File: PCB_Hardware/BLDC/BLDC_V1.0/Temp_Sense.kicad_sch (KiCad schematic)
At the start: 2 parts

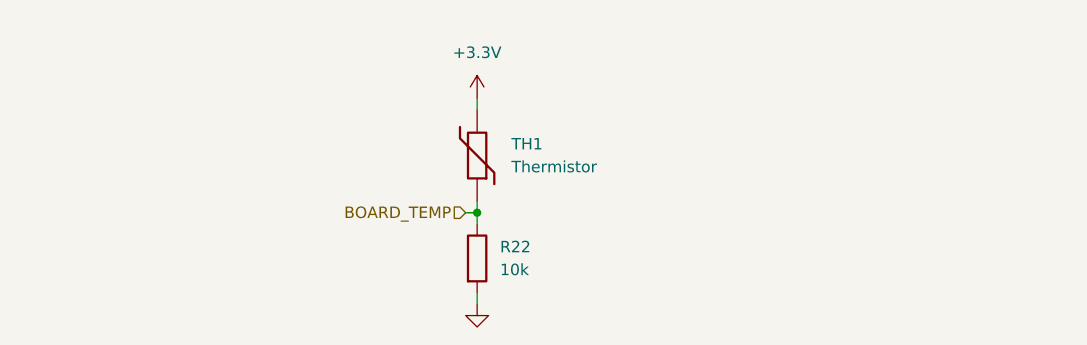
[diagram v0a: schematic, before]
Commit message: redid external temp sensing and instead removed V Bus sense from the USBC input
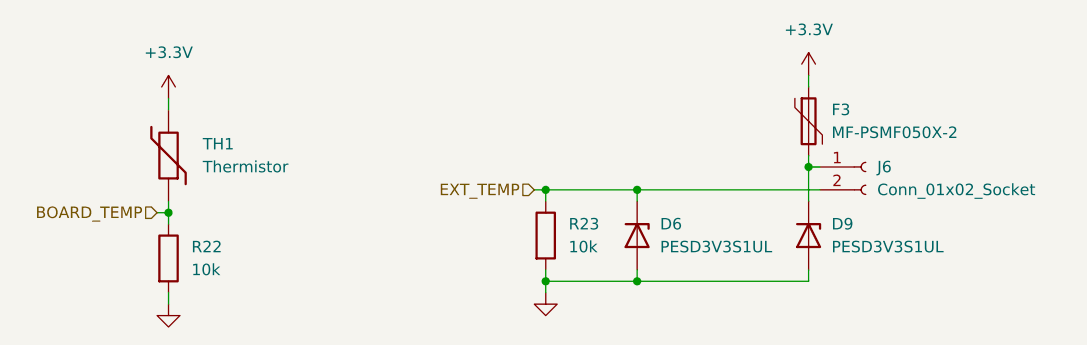
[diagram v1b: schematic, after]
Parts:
- added D6, D9: PESD3V3S1UL, Diode_SMD:D_SOD-882, symbol Diode:PESD3V3S1UL
- added F3: MF-PSMF050X-2, symbol Device:Polyfuse
- added J6: Conn_01x02_Socket, symbol Connector:Conn_01x02_Socket
- added R23: 10k, symbol Device:R
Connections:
- net +3.3V: now also F3.1
- net GND: now also D6.2 (A), D9.2 (A), R23.2
- new net: D9.1 (K), F3.2, J6.1 (Pin_1)
- new net EXT_TEMP: D6.1 (K), J6.2 (Pin_2), R23.1
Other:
- moved on the sheet: R22, TH1

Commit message: Removed external temp sensing bc I forgot the calibration enable pin for the encoder
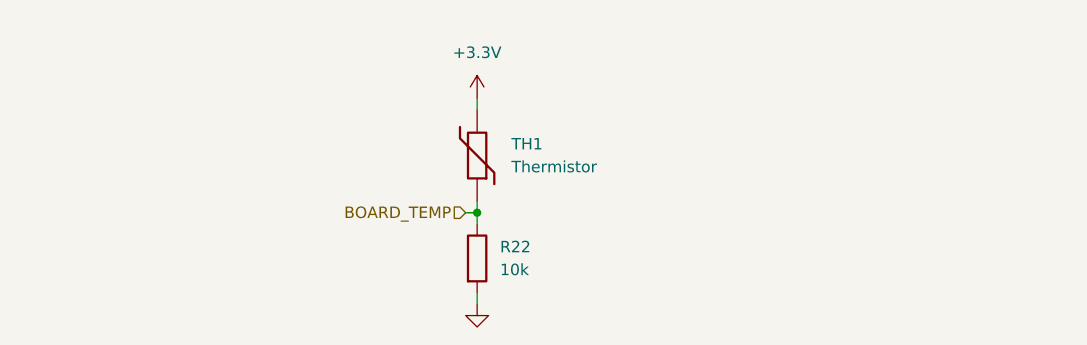
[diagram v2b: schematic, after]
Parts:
- removed D6, D9: PESD3V3S1UL, Diode_SMD:D_SOD-882, symbol Diode:PESD3V3S1UL
- removed F3: MF-PSMF050X-2, symbol Device:Polyfuse
- removed J6: Conn_01x02_Socket, symbol Connector:Conn_01x02_Socket
- removed R23: 10k, symbol Device:R
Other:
- moved on the sheet: R22, TH1
